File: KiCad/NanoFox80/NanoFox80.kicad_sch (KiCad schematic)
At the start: 79 parts, among them J101 Conn_01x02, J102 Conn_01x02, J103 Conn_01x01, J104 Conn_01x02, J105 Conn_01x02, J106 Conn_01x02, J107 Conn_01x02, J108 Conn_01x01, J109 Conn_01x02, J110 I2C, J111 DB9 Female, J112 Conn_01x02, J113 Conn_01x02, J114 Conn_01x02, J115 Conn_01x02, P101 ISP/PDI, Q102 BSS138, SW101 SW_SPST, U101 UCC27517DBVR, U102 LP2985-3.3, U104 74HC4046, U105 AVR128DA28, U106 74HC390, U107 74HC390, U108 LP2985-5.0, U109 TXB0102DCU, X101 SIT1566AC TCO

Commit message: Schematic, BOM and PCB Updates
o Changed parts spec'd for Q101 and Q102
o Updated footprints
o Updated PCB
o Updated Gerbers
o Updated BOM
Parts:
- removed Q101: (no value), symbol Transistor_FET:BSS84T116
- added Q101: (no value), symbol Transistor_FET:BSS84
- Q102: value BSS138 -> (none); footprint Package_TO_SOT_SMD:SOT-23 -> (none); Digi-Key Part No. BSS138CT-ND -> BSS84W-FDICT-ND; Manufacturer onsemi -> Diodes Incorporated; Manufacturer PN BSS138 -> BSS84W-7-F
- U103: value (none) -> LMV721M5; footprint (none) -> Package_TO_SOT_SMD:SOT-23-5
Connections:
- net +BATT: now also Q101.2 (S)
- net at Q102.3 (D), R109.2: now also Q101.1 (G)
- net at R110.2: now also Q101.3 (D)
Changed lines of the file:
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@@
   (junction (at 80.01 152.4) (diameter 0) (color 0 0 0 0)
   )
-  (junction (at 43.18 152.4) (diameter 0) (color 0 0 0 0)
-  )
-  (junction (at 50.8 157.48) (diameter 0) (color 0 0 0 0)
-  )
   (junction (at 62.23 63.5) (diameter 0) (color 0 0 0 0)
   )
@@
   (junction (at 118.11 121.92) (diameter 0) (color 0 0 0 0)
   )
+  (junction (at 43.18 152.4) (diameter 0) (color 0 0 0 0)
+  )
   (junction (at 157.48 20.32) (diameter 0) (color 0 0 0 0)
   )
@@
   (junction (at 257.81 29.21) (diameter 0) (color 0 0 0 0)
   )
+  (junction (at 50.8 157.48) (diameter 0) (color 0 0 0 0)
+  )
   (junction (at 246.38 29.21) (diameter 0) (color 0 0 0 0)
   )
@@
     (stroke (width 0) (type default) (color 0 0 0 0))
   )
-  (wire (pts (xy 43.18 152.4) (xy 59.69 152.4))
+  (wire (pts (xy 40.64 152.4) (xy 43.18 152.4))
     (stroke (width 0) (type default) (color 0 0 0 0))
   )
@@
     (stroke (width 0) (type default) (color 0 0 0 0))
   )
-  (wire (pts (xy 40.64 152.4) (xy 43.18 152.4))
-    (stroke (width 0) (type default) (color 0 0 0 0))
-  )
   (wire (pts (xy 43.18 180.34) (xy 43.18 181.61))
     (stroke (width 0) (type default) (color 0 0 0 0))
@@
     (stroke (width 0) (type default) (color 0 0 0 0))
   )
+  (wire (pts (xy 43.18 152.4) (xy 59.69 152.4))
+    (stroke (width 0) (type default) (color 0 0 0 0))
+  )
   (wire (pts (xy 125.73 138.43) (xy 130.81 138.43))
     (stroke (width 0) (type default) (color 0 0 0 0))
@@
     (pin "2")
   )
+  (symbol (lib_id "Transistor_FET:BSS84") (at 45.72 157.48 180) (unit 1)
+    (in_bom yes) (on_board yes) (fields_autoplaced)
+    (property "Reference" "Q101" (id 0) (at 40.5131 156.6453 0)
+      (effects (font (size 1.27 1.27)) (justify left))
+    )
+    (property "Value" "" (id 1) (at 40.5131 159.1822 0)
+      (effects (font (size 1.27 1.27)) (justify left))
+    )
+    (property "Footprint" "" (id 2) (at 40.64 155.575 0)
+      (effects (font (size 1.27 1.27) italic) (justify left) hide)
+    )
+    (property "Datasheet" "" (id 3) (at 45.72 157.48 0)
+      (effects (font (size 1.27 1.27)) (justify left) hide)
+    )
+    (property "Digi-Key Part No." "BSS84W-FDICT-ND" (id 4) (at 45.72 157.48 0)
+      (effects (font (size 1.27 1.27)) hide)
+    )
+    (property "Manufacturer" "Diodes Incorporated" (id 5) (at 45.72 157.48 0)
+      (effects (font (size 1.27 1.27)) hide)
+    )
+    (property "Manufacturer PN" "BSS84W-7-F" (id 6) (at 45.72 157.48 0)
+      (effects (font (size 1.27 1.27)) hide)
+    )
+    (property "Description" "MOSFET P-CH 50V 130MA SOT323" (id 7) (at 45.72 157.48 0)
+      (effects (font (size 1.27 1.27)) hide)
+    )
+    (pin "1")
+    (pin "2")
+    (pin "3")
+  )
   (symbol (lib_id "Device:Battery") (at 35.56 152.4 270) (unit 1)
     (in_bom yes) (on_board yes)
@@
       (effects (font (size 1.54 1.54) bold))
     )
-    (property "Value" "" (id 1) (at 204.47 62.23 0)
+    (property "Value" "LMV721M5" (id 1) (at 204.47 62.23 0)
       (effects (font (size 1.54 1.54) bold))
     )
-    (property "Footprint" "" (id 2) (at 194.31 64.77 0)
+    (property "Footprint" "Package_TO_SOT_SMD:SOT-23-5" (id 2) (at 194.31 64.77 0)
       (effects (font (size 1.27 1.27)) (justify left) hide)
     )
@@
     (pin "2")
   )
-  (symbol (lib_id "Transistor_FET:BSS84T116") (at 45.72 157.48 180) (unit 1)
-    (in_bom yes) (on_board yes) (fields_autoplaced)
-    (property "Reference" "Q101" (id 0) (at 40.5131 156.6453 0)
-      (effects (font (size 1.27 1.27)) (justify left))
-    )
-    (property "Value" "" (id 1) (at 40.5131 159.1822 0)
-      (effects (font (size 1.27 1.27)) (justify left))
-    )
-    (property "Footprint" "" (id 2) (at 40.64 155.575 0)
-      (effects (font (size 1.27 1.27) italic) (justify left) hide)
-    )
-    (property "Datasheet" "http://assets.nexperia.com/documents/data-sheet/BSS84.pdf" (id 3) (at 45.72 157.48 0)
-      (effects (font (size 1.27 1.27)) (justify left) hide)
-    )
-    (property "Digi-Key Part No." "846-BSS84T116CT-ND" (id 4) (at 45.72 157.48 0)
-      (effects (font (size 1.27 1.27)) hide)
-    )
-    (property "Manufacturer" "Rohm Semiconductor" (id 5) (at 45.72 157.48 0)
-      (effects (font (size 1.27 1.27)) hide)
-    )
-    (property "Manufacturer PN" "BSS84T116" (id 6) (at 45.72 157.48 0)
-      (effects (font (size 1.27 1.27)) hide)
-    )
-    (property "Description" "MOSFET P-CH 60V 230MA SST3" (id 7) (at 45.72 157.48 0)
-      (effects (font (size 1.27 1.27)) hide)
-    )
-    (pin "1")
-    (pin "2")
-    (pin "3")
-  )
   (symbol (lib_id "Device:C_Small") (at 96.52 173.99 90) (mirror x) (unit 1)
     (in_bom yes) (on_board yes)
@@
       (effects (font (size 1.27 1.27)) (justify left))
     )
-    (property "Value" "BSS138" (id 1) (at 59.69 173.99 0)
+    (property "Value" "" (id 1) (at 67.31 173.99 0)
       (effects (font (size 1.27 1.27)) (justify left))
     )
-    (property "Footprint" "Package_TO_SOT_SMD:SOT-23" (id 2) (at 48.26 170.815 0)
+    (property "Footprint" "" (id 2) (at 48.26 170.815 0)
       (effects (font (size 1.27 1.27) italic) (justify left) hide)
     )
-    (property "Datasheet" "https://www.onsemi.com/pub/Collateral/BSS138-D.PDF" (id 3) (at 53.34 168.91 0)
+    (property "Datasheet" "https://www.diodes.com/assets/Datasheets/BSS84W.pdf" (id 3) (at 53.34 168.91 0)
       (effects (font (size 1.27 1.27)) (justify left) hide)
     )
-    (property "Digi-Key Part No." "BSS138CT-ND" (id 4) (at 53.34 168.91 0)
+    (property "Digi-Key Part No." "BSS84W-FDICT-ND" (id 4) (at 53.34 168.91 0)
       (effects (font (size 1.27 1.27)) hide)
     )
-    (property "Manufacturer" "onsemi" (id 5) (at 53.34 168.91 0)
+    (property "Manufacturer" "Diodes Incorporated" (id 5) (at 53.34 168.91 0)
       (effects (font (size 1.27 1.27)) hide)
     )
-    (property "Manufacturer PN" "BSS138" (id 6) (at 53.34 168.91 0)
+    (property "Manufacturer PN" "BSS84W-7-F" (id 6) (at 53.34 168.91 0)
       (effects (font (size 1.27 1.27)) hide)
     )
-    (property "Description" "MOSFET N-CH 50V 220MA SOT23-3" (id 7) (at 53.34 168.91 0)
+    (property "Description" "MOSFET P-CH 50V 130MA SOT323" (id 7) (at 53.34 168.91 0)
       (effects (font (size 1.27 1.27)) hide)
     )
@@
       (reference "P101") (unit 1) (value "ISP/PDI") (footprint "Connector_PinHeader_2.54mm:PinHeader_2x03_P2.54mm_Vertical_SMD")
     )
-    (path "/a295d13a-ff5b-4b53-92ad-a66323f160b9"
-      (reference "Q101") (unit 1) (value "BSS84T116") (footprint "Package_TO_SOT_SMD:SOT-23")
+    (path "/06bbe3d7-7cbc-4293-aa1a-7cb3a9e9e8b9"
+      (reference "Q101") (unit 1) (value "BSS84W-7-F") (footprint "Package_TO_SOT_SMD:SOT-323_SC-70")
     )
     (path "/c8819402-7151-4b21-9689-27976a72a03f"
-      (reference "Q102") (unit 1) (value "BSS138") (footprint "Package_TO_SOT_SMD:SOT-23")
+      (reference "Q102") (unit 1) (value "BSS138W-7-F") (footprint "Package_TO_SOT_SMD:SOT-323_SC-70")
     )
     (path "/8c1e669c-9eae-4110-b451-39841b9a0c11"

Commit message: Corrected Q102
Wrong part was specified for Q102.
Set to BSS138W-7-F and updated BOM
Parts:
- Q101: value (none) -> BSS84W-7-F; footprint (none) -> Package_TO_SOT_SMD:SOT-323_SC-70
- Q102: Digi-Key Part No. BSS84W-FDICT-ND -> BSS138W-FDICT-ND; Manufacturer PN BSS84W-7-F -> BSS138W-7-F
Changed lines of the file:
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@@
       (effects (font (size 1.27 1.27)) (justify left))
     )
-    (property "Value" "" (id 1) (at 40.5131 159.1822 0)
-      (effects (font (size 1.27 1.27)) (justify left))
-    )
-    (property "Footprint" "" (id 2) (at 40.64 155.575 0)
+    (property "Value" "BSS84W-7-F" (id 1) (at 40.5131 159.1822 0)
+      (effects (font (size 1.27 1.27)) (justify left))
+    )
+    (property "Footprint" "Package_TO_SOT_SMD:SOT-323_SC-70" (id 2) (at 40.64 155.575 0)
       (effects (font (size 1.27 1.27) italic) (justify left) hide)
     )
@@
       (effects (font (size 1.27 1.27) italic) (justify left) hide)
     )
-    (property "Datasheet" "https://www.diodes.com/assets/Datasheets/BSS84W.pdf" (id 3) (at 53.34 168.91 0)
+    (property "Datasheet" "https://www.diodes.com/assets/Datasheets/BSS138W.pdf" (id 3) (at 53.34 168.91 0)
       (effects (font (size 1.27 1.27)) (justify left) hide)
     )
-    (property "Digi-Key Part No." "BSS84W-FDICT-ND" (id 4) (at 53.34 168.91 0)
+    (property "Digi-Key Part No." "BSS138W-FDICT-ND" (id 4) (at 53.34 168.91 0)
       (effects (font (size 1.27 1.27)) hide)
     )
@@
       (effects (font (size 1.27 1.27)) hide)
     )
-    (property "Manufacturer PN" "BSS84W-7-F" (id 6) (at 53.34 168.91 0)
-      (effects (font (size 1.27 1.27)) hide)
-    )
-    (property "Description" "MOSFET P-CH 50V 130MA SOT323" (id 7) (at 53.34 168.91 0)
-      (effects (font (size 1.27 1.27)) hide)
-    )
+    (property "Manufacturer PN" "BSS138W-7-F" (id 6) (at 53.34 168.91 0)
+      (effects (font (size 1.27 1.27)) hide)
+    )
+    (property "Description" "MOSFET N-CH 50V 200MA SOT323" (id 7) (at 53.34 168.91 0)
+      (effects (font (size 1.27 1.27)) hide)
+    )

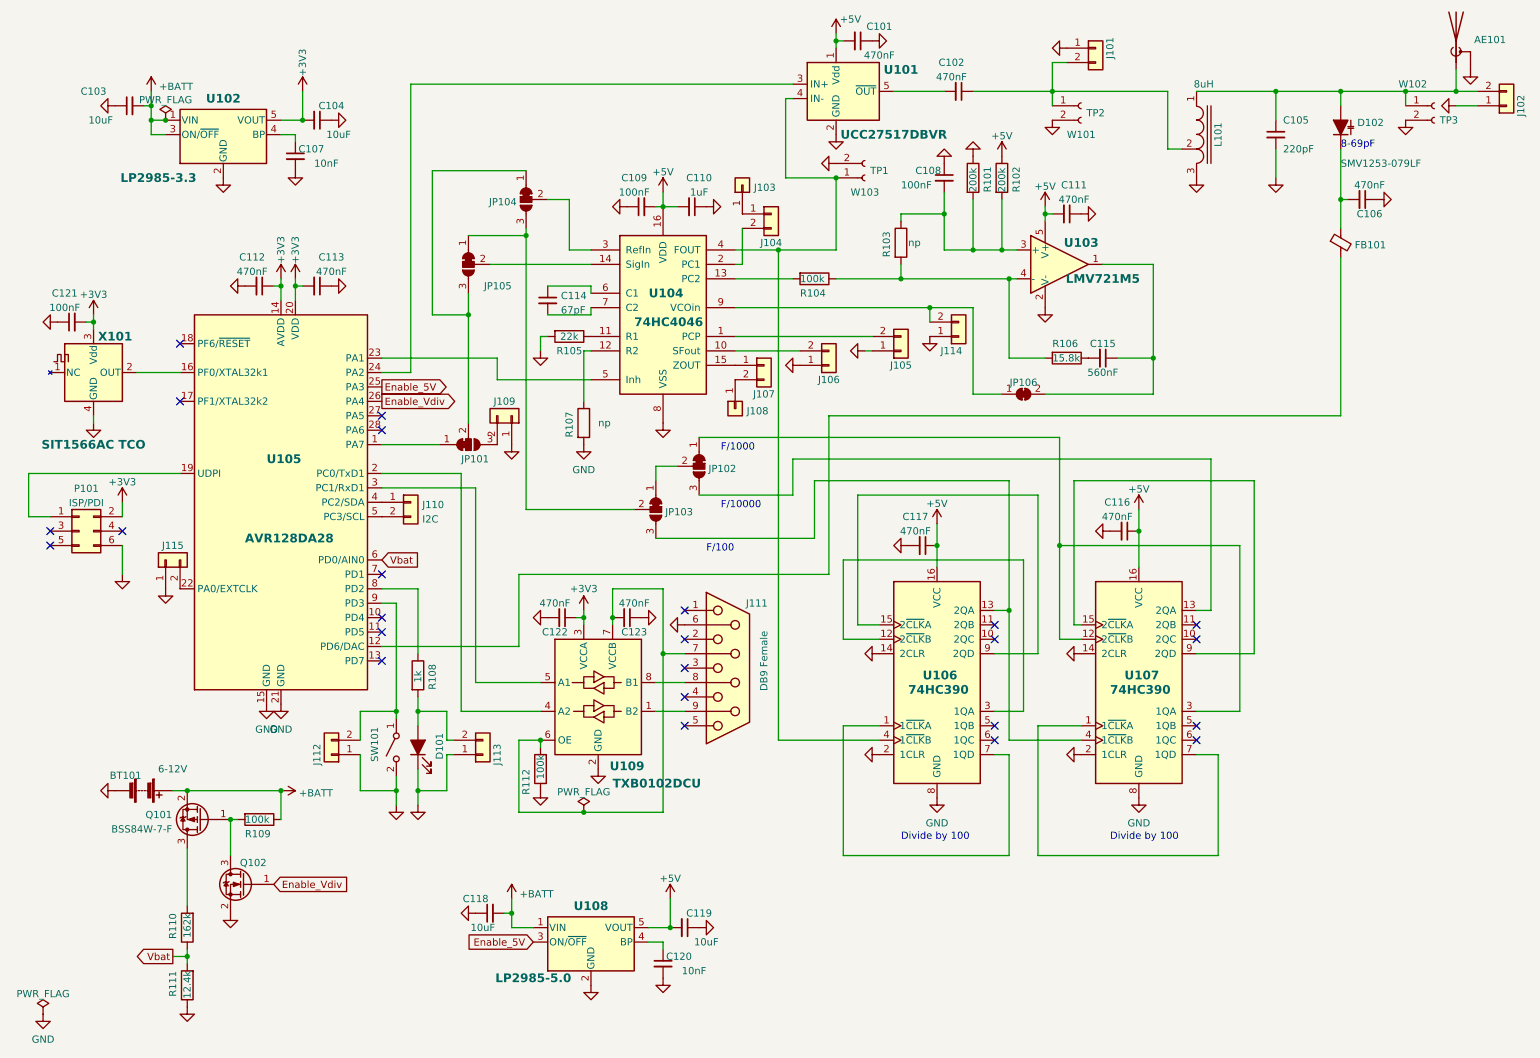
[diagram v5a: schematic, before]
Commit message: Development for Si5351
First changes for Si5351 design approach
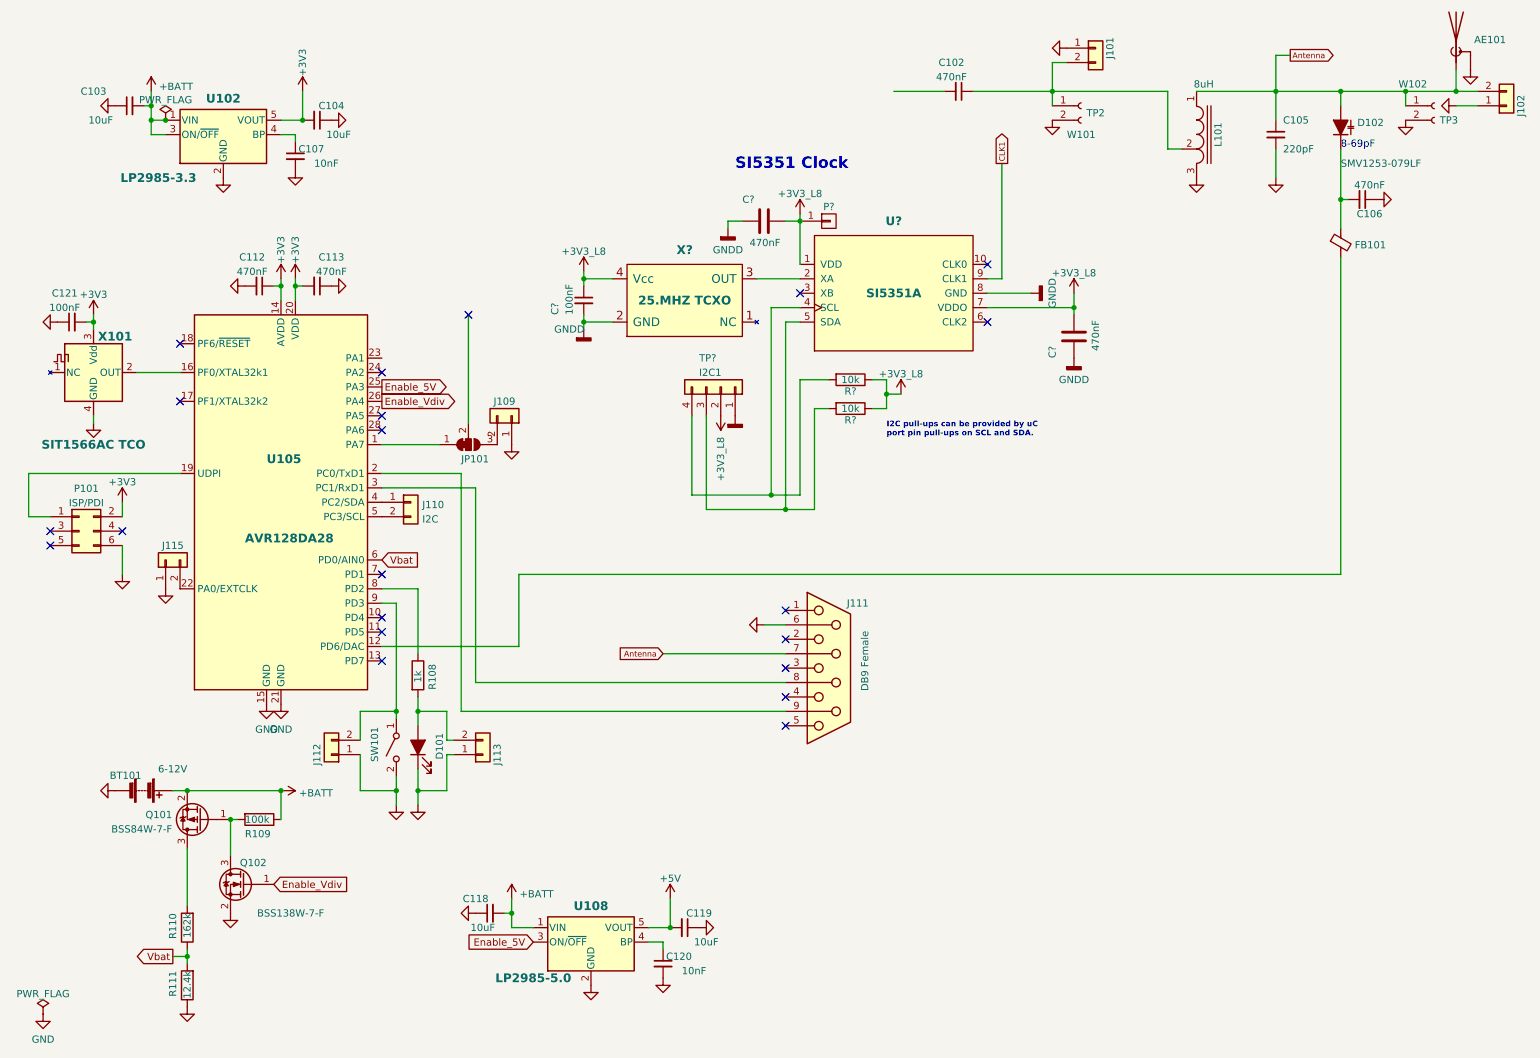
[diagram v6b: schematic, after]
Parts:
- removed C101, C111, C116, C117, C122, C123: 470nF, Capacitor_SMD:C_0805_2012Metric_Pad1.18x1.45mm_HandSolder, symbol Device:C_Small
- removed C108, C109: 100nF, Capacitor_SMD:C_0805_2012Metric_Pad1.18x1.45mm_HandSolder, symbol Device:C_Small
- removed C110: 1uF, Capacitor_SMD:C_0805_2012Metric_Pad1.18x1.45mm_HandSolder, symbol Device:C_Small
- removed C114: 67pF, Capacitor_SMD:C_0805_2012Metric_Pad1.18x1.45mm_HandSolder, symbol Device:C_Small
- removed C115: 560nF, Capacitor_SMD:C_0805_2012Metric_Pad1.18x1.45mm_HandSolder, symbol Device:C_Small
- removed J103, J108: Conn_01x01, Connector_PinSocket_2.54mm:PinSocket_1x01_P2.54mm_Vertical, symbol Connector_Generic:Conn_01x01
- removed J104, J105, J106, J107, J114: Conn_01x02, Connector_PinSocket_2.54mm:PinSocket_1x02_P2.54mm_Vertical, symbol Connector_Generic:Conn_01x02
- removed JP102, JP103, JP104, JP105: SolderJumper_3_Bridged12, Jumper:SolderJumper-3_P1.3mm_Bridged12_RoundedPad1.0x1.5mm_NumberLabels, symbol Jumper:SolderJumper_3_Bridged12
- removed JP106: SolderJumper_2_Bridged, Jumper:SolderJumper-2_P1.3mm_Bridged_RoundedPad1.0x1.5mm, symbol Jumper:SolderJumper_2_Bridged
- removed R101, R102: 200k, Resistor_SMD:R_0805_2012Metric_Pad1.20x1.40mm_HandSolder, symbol Device:R
- removed R103, R107: np, Resistor_SMD:R_0805_2012Metric_Pad1.20x1.40mm_HandSolder, symbol Device:R
- removed R104, R112: 100k, Resistor_SMD:R_0805_2012Metric_Pad1.20x1.40mm_HandSolder, symbol Device:R
- removed R105: 22k, Resistor_SMD:R_0805_2012Metric_Pad1.20x1.40mm_HandSolder, symbol Device:R
- removed R106: 15.8k, Resistor_SMD:R_0805_2012Metric_Pad1.20x1.40mm_HandSolder, symbol Device:R
- removed U101: UCC27517DBVR, Package_TO_SOT_SMD:SOT-23-5, symbol Driver_FET:UCC27517DBVR
- removed U103: LMV721M5, Package_TO_SOT_SMD:SOT-23-5, symbol Amplifier_Operational:OPA197xDBV
- removed U104: 74HC4046, Package_SO:SOIC-16W_5.3x10.2mm_P1.27mm, symbol 4xxx:4046
- removed U106, U107: 74HC390, Package_SO:SOIC-16W_5.3x10.2mm_P1.27mm, symbol 74xx:74HC390
- removed U109: TXB0102DCU, Package_SO:VSSOP-8_2.4x2.1mm_P0.5mm, symbol Logic_LevelTranslator:TXB0102DCU
- removed W103: TP1, Measurement:Measurement_Point_ScopeProbe_Round-SMD-2sides-Pad_Small, symbol Connector:Conn_01x02_Female
- added C? (x2): 470nF, Capacitors_SMD:C_0805, symbol Device:C
- added C?: 100nF, Capacitors_SMD:C_0805, symbol Device:C_Small
- added P?: Thru, Pin_Headers:Pin_Header_Straight_1x01, symbol FlexFox80-rescue:CONN_01X01-ARDF-2-Band-MiniTx-rescue
- added R? (x2): 10k, Resistors_SMD:R_0805, symbol Device:R
- added TP?: I2C1, Pin_Headers:Pin_Header_Straight_1x04, symbol Connector_Generic:Conn_01x04
- added U?: SI5351A, Housings_SSOP:MSOP-10_3x3mm_Pitch0.5mm, symbol special:SI5351
- added X?: 25.MHZ TCXO, Crystals:ASTX-H11-25.000MHZ, symbol special:ASTX-H11
- Q102: value (none) -> BSS138W-7-F; footprint (none) -> Package_TO_SOT_SMD:SOT-323_SC-70
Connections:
- net Antenna: now reaches AE101.2 (A), C105.1, D102.2 (A), J102.2 (Pin_2), L101.1, W102.1 (Pin_1)
- net Antenna: now also J111.7
- net at J111.9: now also U105.2 (PC0/TxD1)
- net at U105.3 (PC1/RxD1): now also J111.8
- new net: U?.2 (XA), X?.3 (OUT)
- new net: R?.2, TP?.4 (Pin_4), U?.4 (SCL)
- new net: R?.2, TP?.3 (Pin_3), U?.5 (SDA)
- new net +3V3_L8: C?.1, C?.1, C?.1, P?.1 (P1), R?.1, R?.1, TP?.2 (Pin_2), U?.1 (VDD), U?.7 (VDDO), X?.4 (Vcc)
- new net CLK1: U?.9 (CLK1)
- new net GNDD: C?.2, C?.2, C?.2, TP?.1 (Pin_1), U?.8 (GND), X?.2 (GND)
- no-connect marks 24 -> 21
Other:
- note added: "I2C pull-ups can be provided by uC port pin pull-ups on SCL and SDA."
- note added: "SI5351 Clock"
- note removed: "Divide by 100"
- note removed: "F/100"
- note removed: "F/1000"
- note removed: "F/10000"
- moved on the sheet: J111

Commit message: Development
o Schematic updates for Si5351 approach
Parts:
- removed C118, C119: 10uF, Capacitor_SMD:C_0805_2012Metric_Pad1.18x1.45mm_HandSolder, symbol Device:C_Small
- removed C120: 10nF, Capacitor_SMD:C_0805_2012Metric_Pad1.18x1.45mm_HandSolder, symbol Device:C_Small
- removed J110: I2C, Connector_PinHeader_2.54mm:PinHeader_1x02_P2.54_Nonpolarized, symbol Connector_Generic:Conn_01x02
- removed U108: LP2985-5.0, Package_TO_SOT_SMD:SOT-23-5, symbol Regulator_Linear:LP2985-5.0
- added C?: 10nF, Capacitor_SMD:C_0805_2012Metric_Pad1.18x1.45mm_HandSolder, symbol Device:C_Small
- added C? (x2): 10uF, Capacitor_SMD:C_0805_2012Metric_Pad1.18x1.45mm_HandSolder, symbol Device:C_Small
- added U?: LP2985-3.3, Package_TO_SOT_SMD:SOT-23-5, symbol Regulator_Linear:LP2985-3.3
- added U?: MC74VHC1G125, Package_TO_SOT_SMD:TSOT-23-5, symbol 74xx:MC74VHC1G125
- C102: value 470nF -> 100nF
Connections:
- net GND is gone; now on net +3V3_L8: AE101.1 (Shield), BT101.1 (-), C103.1, C104.1, C105.2, C106.1, C107.2, C112.2, C113.1, C121.1, D101.1 (K), J101.1 (Pin_1), J102.1 (Pin_1), J109.1 (Pin_1), J111.6, J112.1 (Pin_1), J113.1 (Pin_1), J115.1 (Pin_1), L101.3, P101.6 (Pin_6), Q102.2 (S), R111.1, SW101.2 (B), U102.2 (GND), U105.15 (GND), U105.21 (GND), W101.2 (Pin_2), W102.2 (Pin_2), X101.4 (GND)
- net +3V3_L8: now also C?.1, C?.1, C?.2, C?.2, U?.2 (GND), U?.3 (GND), U?.5 (VCC), U?.5 (VOUT)
- net +BATT: now also C?.2, U?.1 (VIN)
- net Antenna: now also J111.1; no longer J111.7
- net Enable_Vdiv: no longer U105.26 (PA4)
- net at R?.2, U?.4 (SCL): now also TP?.3 (Pin_3), U105.5 (PC3/SCL); no longer TP?.4 (Pin_4)
- net at R?.2, U?.5 (SDA): now also TP?.4 (Pin_4), U105.4 (PC2/SDA); no longer TP?.3 (Pin_3)
- net at C102.2: now also U?.4 (Y)
- net at U105.23 (PA1): now also U?.1 (~{OE})
- net CLK1: no longer names the net of U?.9 (CLK1)
- net CLK1: now also U?.2 (A)
- net Enable_5V renamed Enable_RF
- net Enable_RF: now also U?.3 (ON/~{OFF})
- new net: C?.1, U?.4 (BP)
- new net V+_Charging: J111.7
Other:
- moved on the sheet: C?, P?, R?, TP?, U?, X?
